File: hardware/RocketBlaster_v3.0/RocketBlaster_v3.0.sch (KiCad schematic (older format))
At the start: 24 parts, among them J0 Conn_02x03_Odd_Even, J1 B2B-XH-A_LF__SN_, J2 B2B-XH-A_LF__SN_, J3 B2B-XH-A_LF__SN_, J4 B2B-XH-A_LF__SN_, J5 B2B-XH-A_LF__SN_, Q1 IRLML6344TRPBF, U1 ATMEGA328PB-AU, U2 LM7805MPX_NOPB, U3 DFR0299

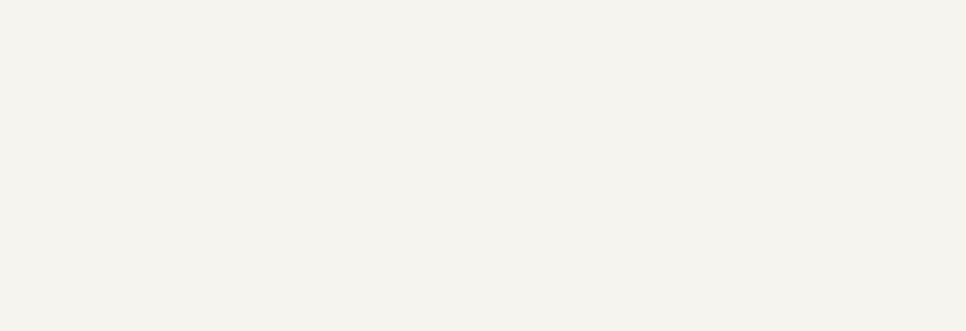
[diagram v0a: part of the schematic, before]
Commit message: Added image for current state of the schematic
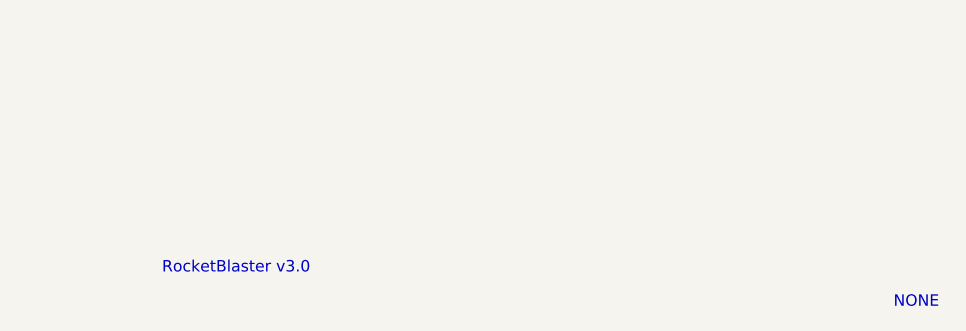
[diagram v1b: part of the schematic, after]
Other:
- note added: "NONE"
- note added: "RocketBlaster v3.0"
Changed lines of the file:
@@
 	1    0    0    -1
 $EndComp
+Text Notes 10600 7650 0    50   ~ 0
+NONE
+Text Notes 7400 7500 0    50   ~ 0
+RocketBlaster v3.0
 $EndSCHEMATC
